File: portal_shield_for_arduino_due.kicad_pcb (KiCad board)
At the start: 2 copper layers, 101.6 x 53.3 mm, 85 parts, among them J1 RS485_1, J2 RS485_2, J3 Sensor, J4 RS485_1_Config, J5 RS485_2_Config, J6 ATX_SEN, J7 RS232_1, J8 RS232_2, P1 Power, P10 CONN_01X01, P11 CONN_01X01, P13 CONN_01X01, P2 Analog, P3 Analog, P4 Digital, P5 PWM, P6 PWM, P7 Communication, P8 CONN_01X01, Q1 BSS123LT1, Q10 FDN340P, Q11 FDN340P, Q2 BSS123LT1, Q3 FDN340P, Q5 FDN340P, Q8 FDN340P, Q9 FDN340P, SW1 SW_UART1, SW2 SW_UART2, U1 MAX481E, U2 LTV-817S, U3 MAX481E, U4 MP1584, U5 LTV-817S, U7 MAX3232

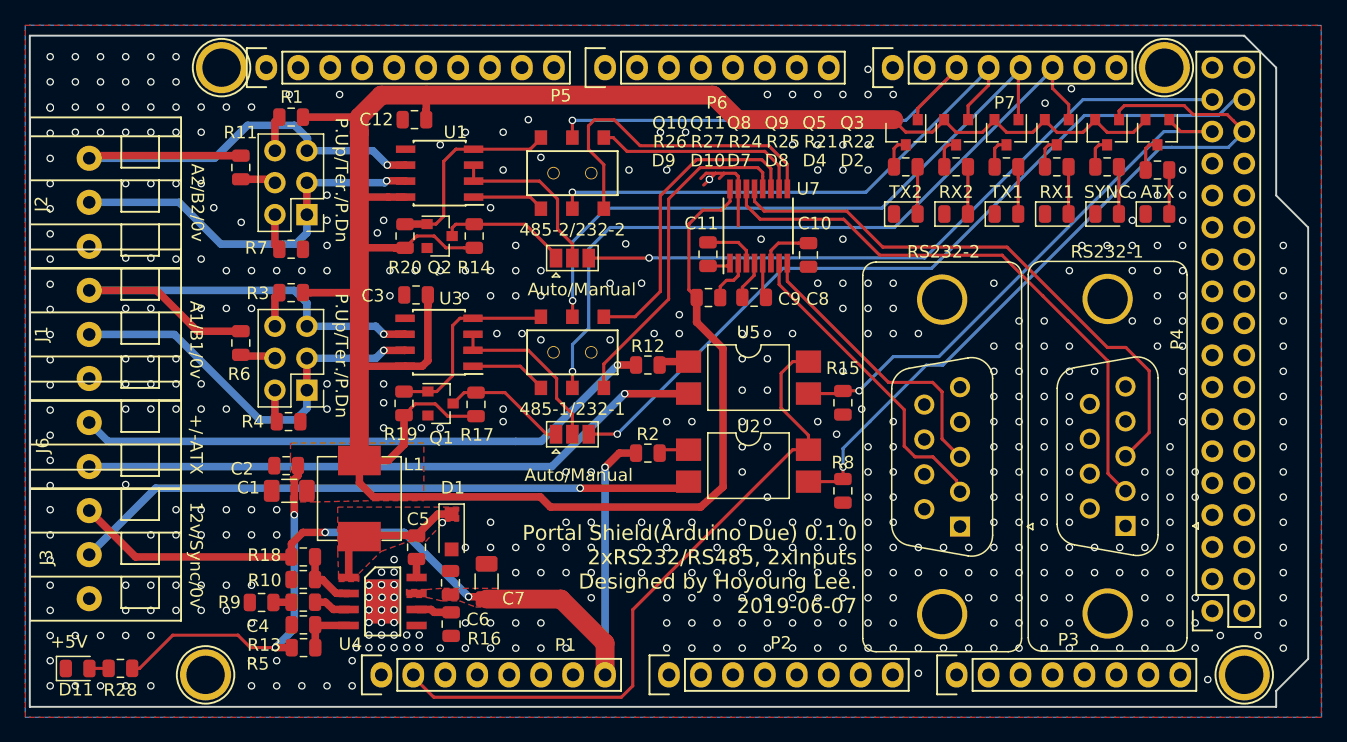
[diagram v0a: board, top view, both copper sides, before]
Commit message: modified to expand the interval between DSUB9s, and add labels of terminals
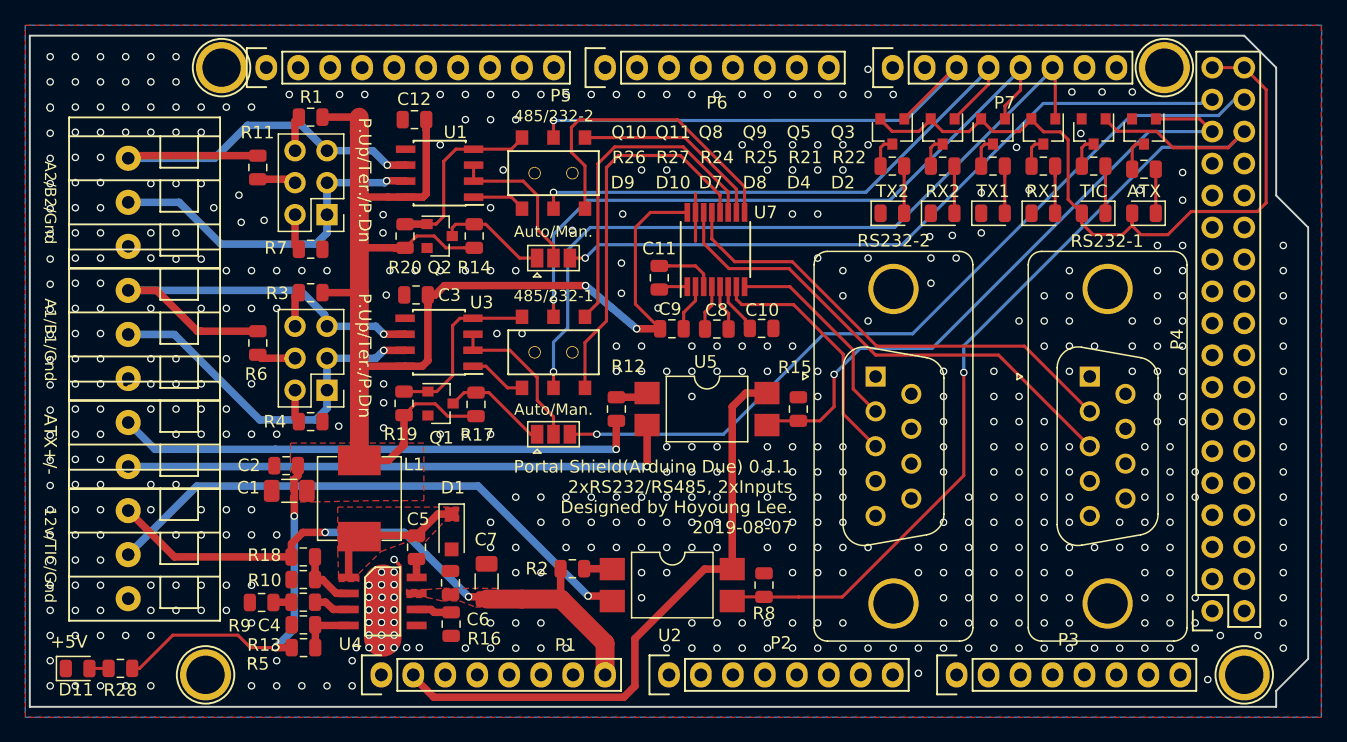
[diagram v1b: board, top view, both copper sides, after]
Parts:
- Q3, Q5: value FDN340P -> BSS123LT1
- moved J8 13.7 mm to (170.6, 95.4), turned to 90 degrees
- moved J7 12.2 mm to (187.6, 95.4), turned to 90 degrees
- moved U2 11.3 mm to (154.4, 112.0)
- moved R2 11.0 mm to (146.5, 110.7)
- moved R8 9.77 mm to (161.7, 112.0), turned to 270 degrees
- moved C10 6.93 mm to (161.5, 91.6), turned to 180 degrees
- moved R12 4.30 mm to (150.0, 98.0), turned to 270 degrees
- moved C11 4.29 mm to (153.4, 87.6)
- moved U5 4.14 mm to (157.2, 98.0)
- moved C8 3.89 mm to (158.0, 91.6)
- moved U7 3.88 mm to (157.9, 85.3)
- moved C9 3.82 mm to (154.4, 91.6)
- moved R15 3.58 mm to (164.5, 98.0), turned to 270 degrees
- moved J1 3.10 mm to (112.5, 92.1)
- moved J2 3.10 mm to (112.5, 81.6)
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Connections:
- D2 pad 1: GND -> Net-(D2-Pad1)
- D2 pad 2: Net-(D2-Pad2) -> +5VP
- D4 pad 1: GND -> Net-(D4-Pad1)
- D4 pad 2: Net-(D4-Pad2) -> +5VP
- Q10 pad 2: +5V -> +5VP
- Q11 pad 2: +5V -> +5VP
- Q3 pad 2: +5V -> GND
- Q5 pad 2: +5V -> GND
- Q8 pad 2: +5V -> +5VP
- Q9 pad 2: +5V -> +5VP
- R21 pad 1: Net-(D4-Pad2) -> Net-(D4-Pad1)
- R22 pad 1: Net-(D2-Pad2) -> Net-(D2-Pad1)
- U7 pad 13: Net-(J7-Pad3) -> Net-(J7-Pad2)
- U7 pad 14: Net-(J7-Pad2) -> Net-(J7-Pad3)
- U7 pad 7: Net-(J8-Pad2) -> Net-(J8-Pad3)
- U7 pad 8: Net-(J8-Pad3) -> Net-(J8-Pad2)
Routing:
- net +5V: track 232.4 -> 141.0 mm, vias 2 -> 4
- net +5VP: track 0.00 -> 57.9 mm
- net /Vin(12V): track 69.3 -> 49.2 mm, vias 3 -> 2
- net /25(SYNC): track 59.3 -> 74.6 mm
- net Net-(J8-Pad2): track 25.0 -> 16.3 mm
- net Net-(J7-Pad2): track 46.1 -> 37.8 mm
- net /24(ATX_SEN): track 44.5 -> 51.5 mm
- net Net-(J7-Pad3): track 45.5 -> 39.8 mm
- net Net-(J3-Pad2): track 50.1 -> 44.5 mm
- net /RS485_A1: track 41.0 -> 35.5 mm
- net /RS485_A2: track 40.3 -> 34.8 mm
- net Net-(J6-Pad1): track 50.0 -> 44.6 mm
- net /IOREF: track 53.6 -> 48.9 mm
- net Net-(J6-Pad2): track 46.6 -> 41.9 mm
- net Net-(D4-Pad2): track 3.75 -> 0.00 mm
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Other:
- board text added: "12v/TIC/Gnd"
- board text added: "485/232-1"
- board text added: "485/232-2"
- board text added: "A1/B1/Gnd"
- board text added: "A2/B2/Gnd"
- board text added: "ATX+/-"
- board text added: "Auto/Man."
- board text added: "Portal Shield(Arduino Due) 0.1.1 2xRS232/RS485, 2xInputs Designed by Hoyoung Lee. 2019-08-07"
- board text added: "TIC"
- board text removed: "+/-ATX"
- board text removed: "12v/Sync/0v"
- board text removed: "485-1/232-1"
- board text removed: "485-2/232-2"
- board text removed: "A1/B1/0v"
- board text removed: "A2/B2/0v"
- board text removed: "Auto/Manual"
- board text removed: "Portal Shield(Arduino Due) 0.1.0 2xRS232/RS485, 2xInputs Designed by Hoyoung Lee. 2019-06-07"
- board text removed: "SYNC"
